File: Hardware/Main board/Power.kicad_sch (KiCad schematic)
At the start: 14 parts, among them U5 AP7361C-33E, U6 AP7361C-33E, U7 AP7361C-33E, U8 AP7361C-33E, U9 TPM8837C

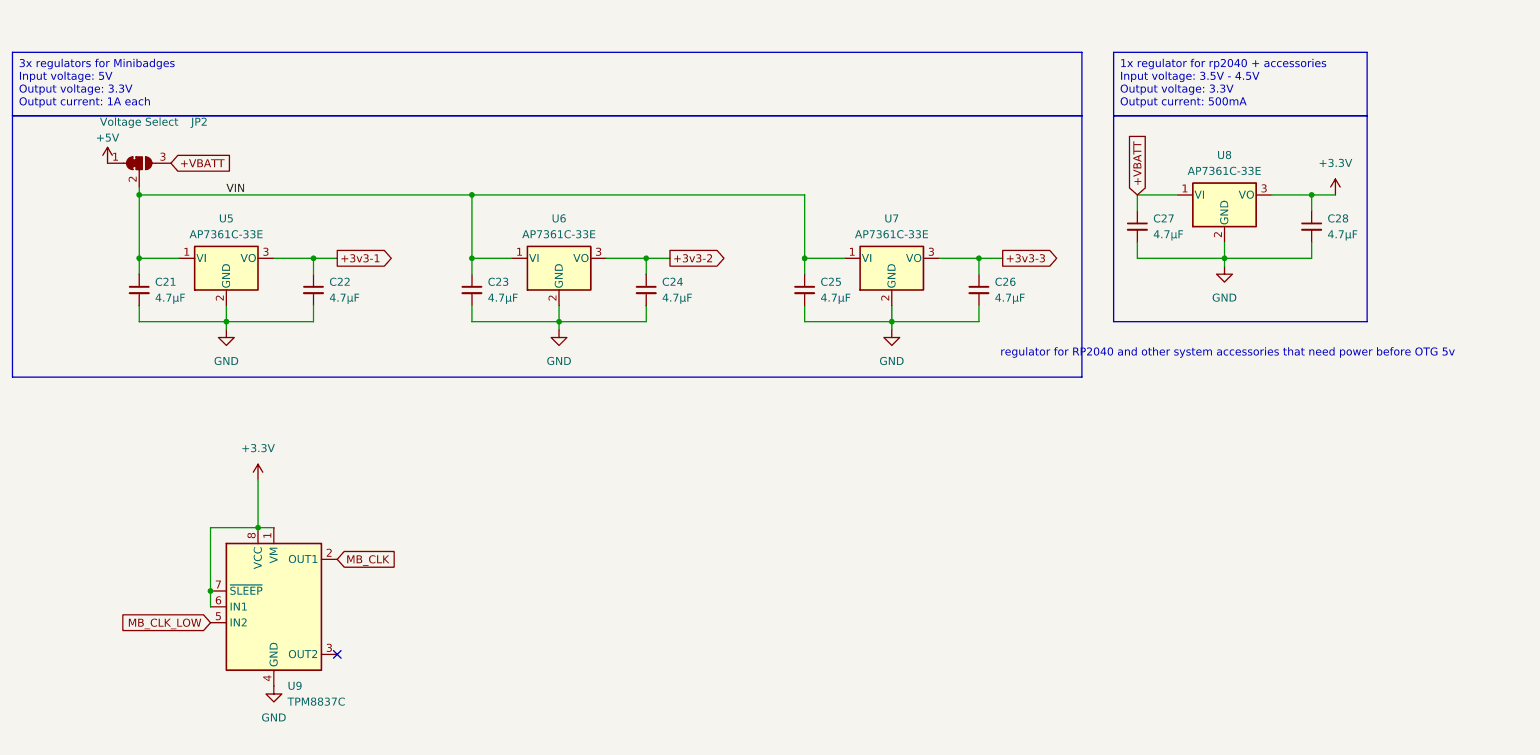
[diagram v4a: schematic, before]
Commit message: Update GND symbols
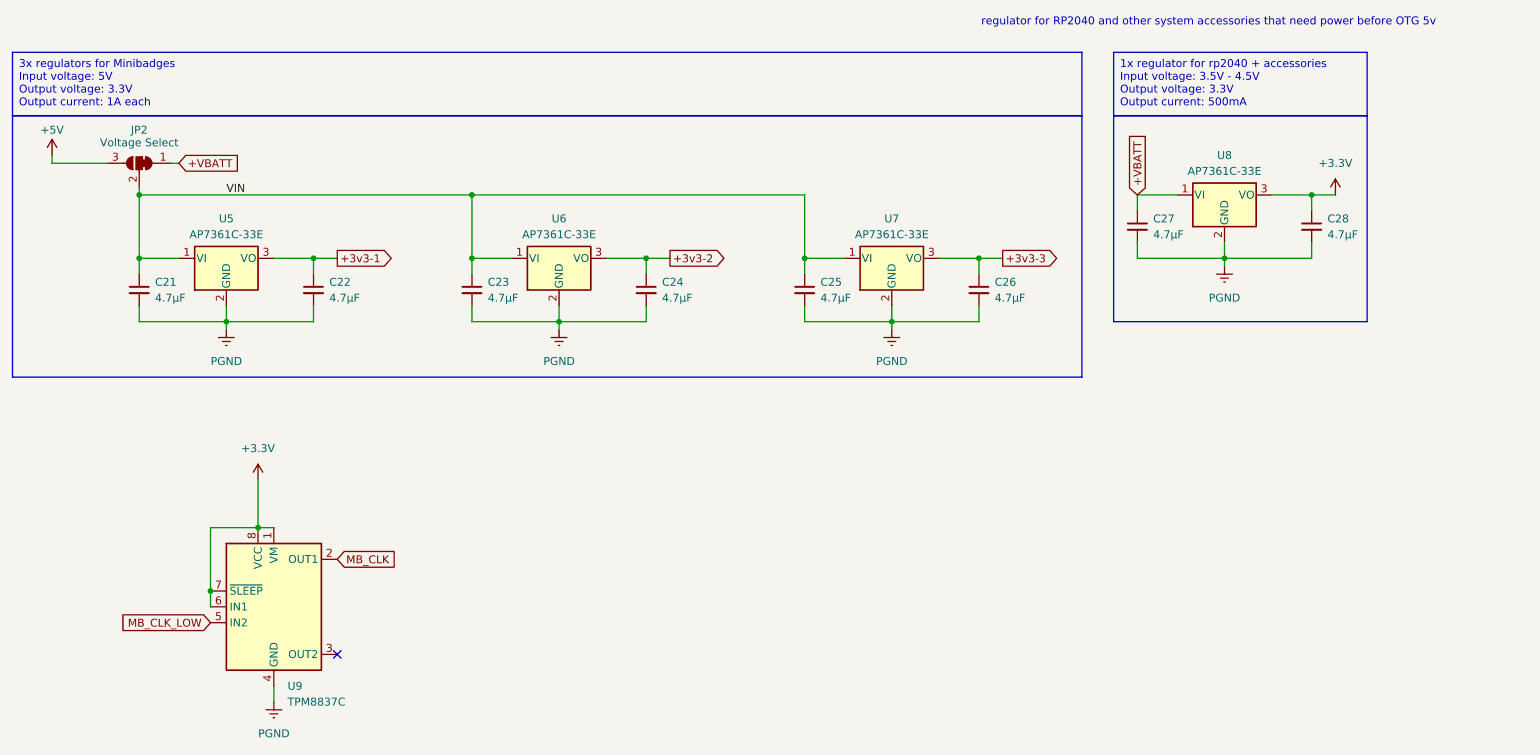
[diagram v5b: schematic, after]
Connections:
- net +5V: now also JP2.3 (B); no longer JP2.1 (A)
- net +VBATT: now also JP2.1 (A); no longer JP2.3 (B)
- net GND renamed PGND

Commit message: refactor PCB for new BMS layout
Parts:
- removed JP2: Voltage Select, Jumper:SolderJumper-3_P1.3mm_Bridged12_Pad1.0x1.5mm_NumberLabels, symbol Jumper:SolderJumper_3_Bridged12
- renumbered C27 to C12, C28 to C13, C21 to C14, C22 to C15, C23 to C16, C24 to C17, C25 to C18, C26 to C19, U8 to U4, U9 to U8
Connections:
- net VIN is gone; now on net +VBATT: C14.1, C16.1, C18.1, U5.1 (VI), U6.1 (VI), U7.1 (VI)
